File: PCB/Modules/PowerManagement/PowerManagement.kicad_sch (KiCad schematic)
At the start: 28 parts, among them J1 USB, J2 BUS, J3 In, J4 PWR, J5 BATT, J6 BUTT, U1 MP2723A, U2 TPS61032

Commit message: Convert all KiCad to 6.0, clean up libraries, remove files that shouldn't be committed.
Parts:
- U1: symbol PowerManagement:MP2723A -> KTANE:MP2723A
- U2: symbol PowerManagement:TPS61032 -> KTANE:TPS61032
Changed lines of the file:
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@@
     (pin "1")
   )
-  (symbol (lib_id "PowerManagement:MP2723A") (at 62.23 43.18 0) (unit 1)
+  (symbol (lib_id "KTANE:MP2723A") (at 62.23 43.18 0) (unit 1)
     (in_bom yes) (on_board yes) (fields_autoplaced)
     (property "Reference" "U1" (id 0) (at 62.23 18.9443 0))
@@
     (pin "1")
   )
-  (symbol (lib_id "PowerManagement:TPS61032") (at 64.135 109.22 0) (unit 1)
+  (symbol (lib_id "KTANE:TPS61032") (at 64.135 109.22 0) (unit 1)
     (in_bom yes) (on_board yes) (fields_autoplaced)
     (property "Reference" "U2" (id 0) (at 63.8175 90.6993 0))

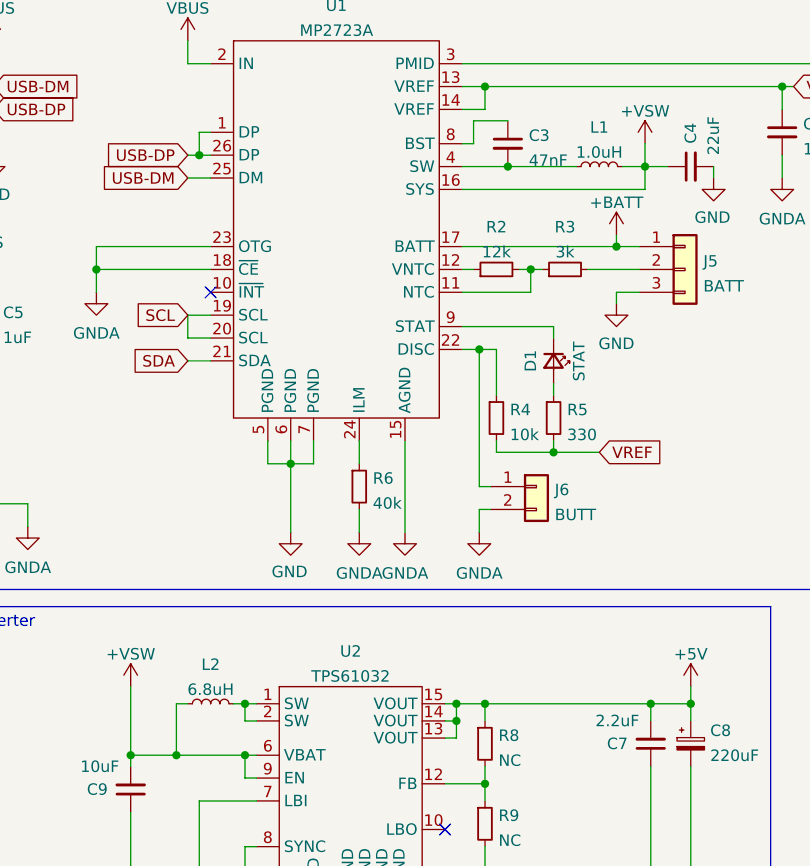
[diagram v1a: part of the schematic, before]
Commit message: Upgrade KiCad files from 6.0 to 7.0.
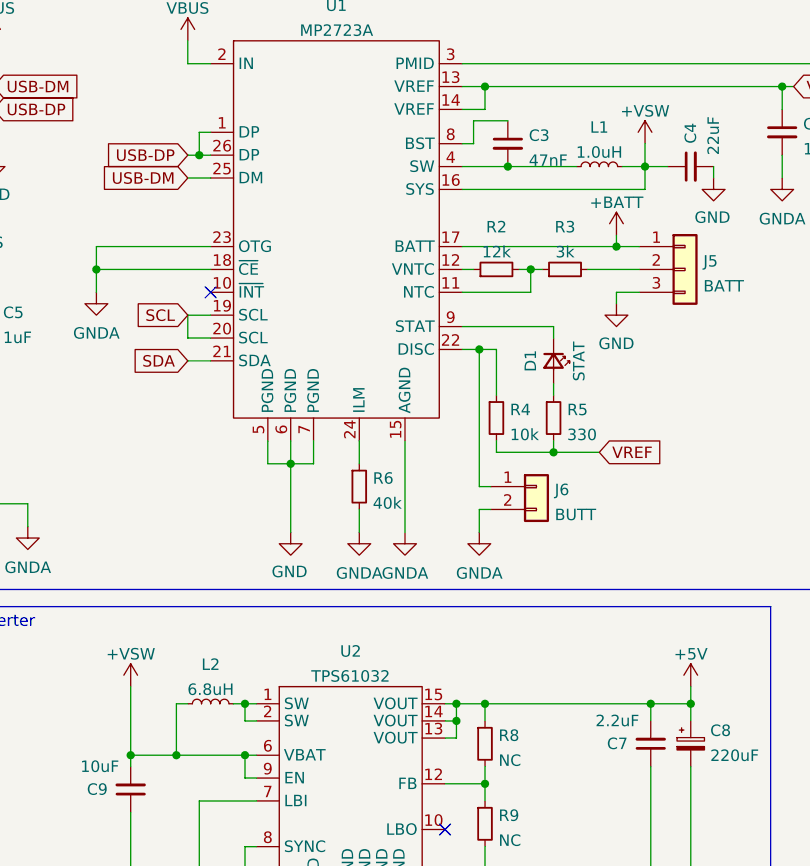
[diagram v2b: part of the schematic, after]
